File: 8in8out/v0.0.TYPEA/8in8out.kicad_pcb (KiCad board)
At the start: 2 copper layers, 100.1 x 86.4 mm, 63 parts, among them IC1 ATTINY48-A, J1 RJ45, J2 RJ45, J3 CONN_6, K110 G5T-1-12VDC, K120 G5T-1-12VDC, K130 G5T-1-12VDC, K140 G5T-1-12VDC, K150 G5T-1-12VDC, K160 G5T-1-12VDC, K170 G5T-1-12VDC, K180 G5T-1-12VDC, P1 CONN_5, P100 CONN_2, P101 CONN_2, P102 CONN_2, P103 CONN_2, P105 CONN_2, P106 CONN_2, P110 CONN_2, P120 CONN_2, P130 CONN_2, P140 CONN_2, P150 CONN_2, P160 CONN_2, P170 CONN_2, P180 CONN_2, P2 CONN_5, P3 CONN_10X2, P4 CONN_2, U1 7805, U10 OPTO-TRANSISTOR, U2 ULN2803, U20 OPTO-TRANSISTOR, U30 OPTO-TRANSISTOR, U40 OPTO-TRANSISTOR, U50 OPTO-TRANSISTOR, U60 OPTO-TRANSISTOR, U70 OPTO-TRANSISTOR, U80 OPTO-TRANSISTOR

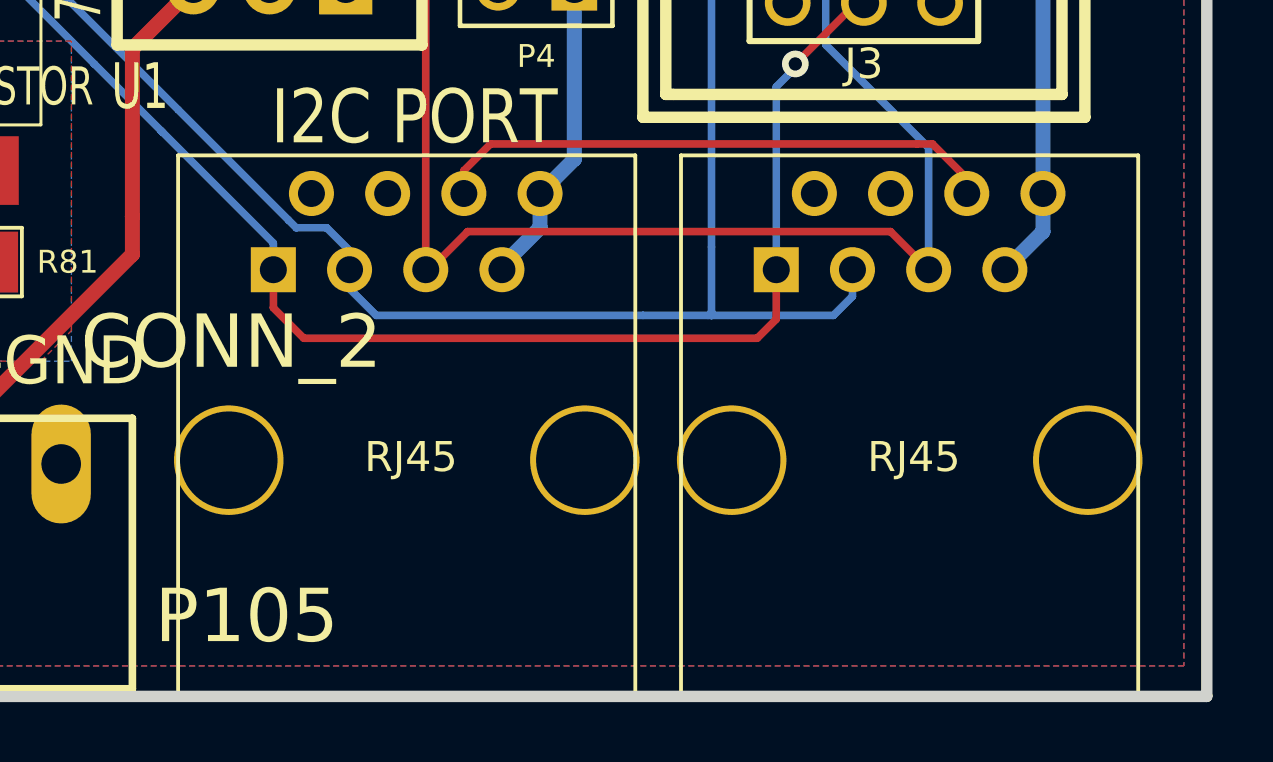
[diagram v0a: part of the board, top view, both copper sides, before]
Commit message: correction empreinte relais (inversion broches du contact) correction empreinte RJ45 (ajout percage shield)
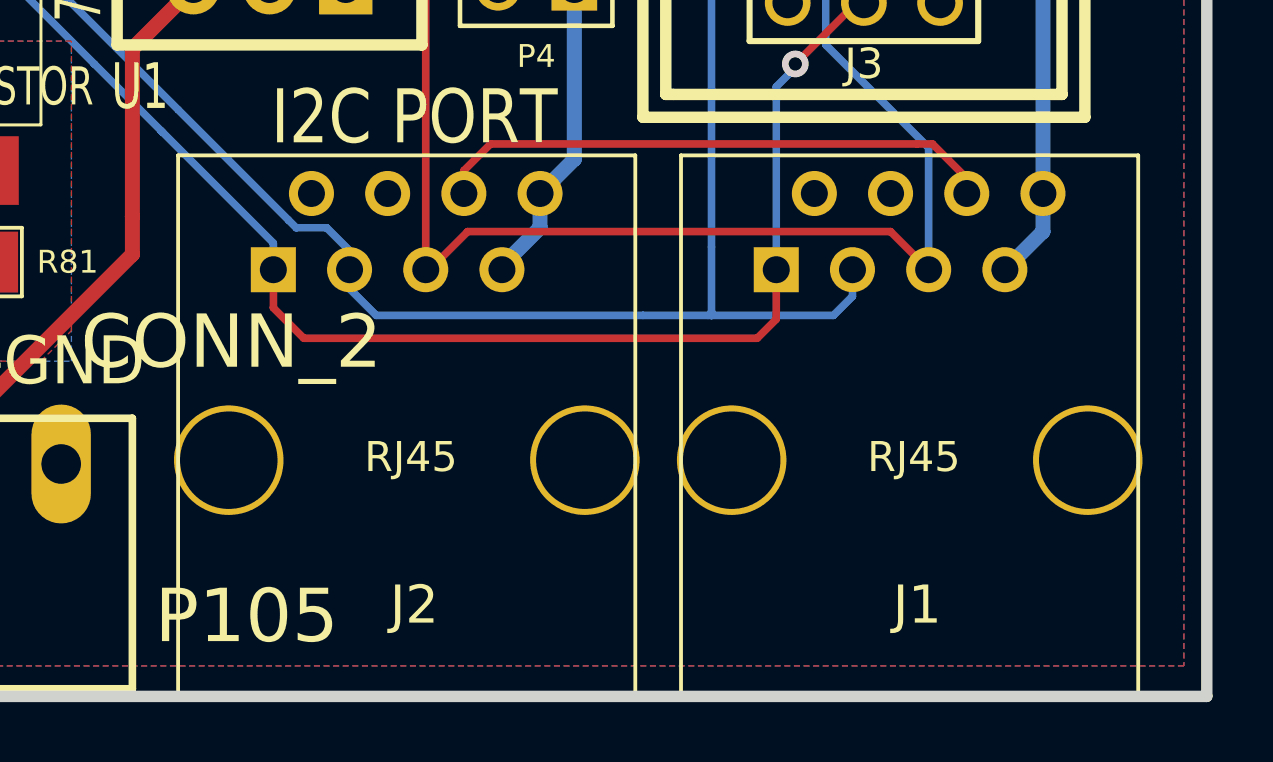
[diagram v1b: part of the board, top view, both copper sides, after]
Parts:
- J1, J2: footprint RJ45_8 -> RJ45_BASIC
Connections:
- J3 pad 6: (no net) -> N-0000091
- U10 pad 3: (no net) -> N-0000076
- U10 pad 6: (no net) -> N-0000077
- U20 pad 3: (no net) -> N-0000083
- U20 pad 6: (no net) -> N-0000084
- U30 pad 3: (no net) -> N-0000086
- U30 pad 6: (no net) -> N-0000087
- U40 pad 3: (no net) -> N-0000057
- U40 pad 6: (no net) -> N-0000058
- U50 pad 3: (no net) -> N-0000059
- U50 pad 6: (no net) -> N-0000060
- U60 pad 3: (no net) -> N-0000063
- U60 pad 6: (no net) -> N-0000048
- U70 pad 3: (no net) -> N-0000050
- U70 pad 6: (no net) -> N-0000051
- U80 pad 3: (no net) -> N-0000053
- U80 pad 6: (no net) -> N-0000054

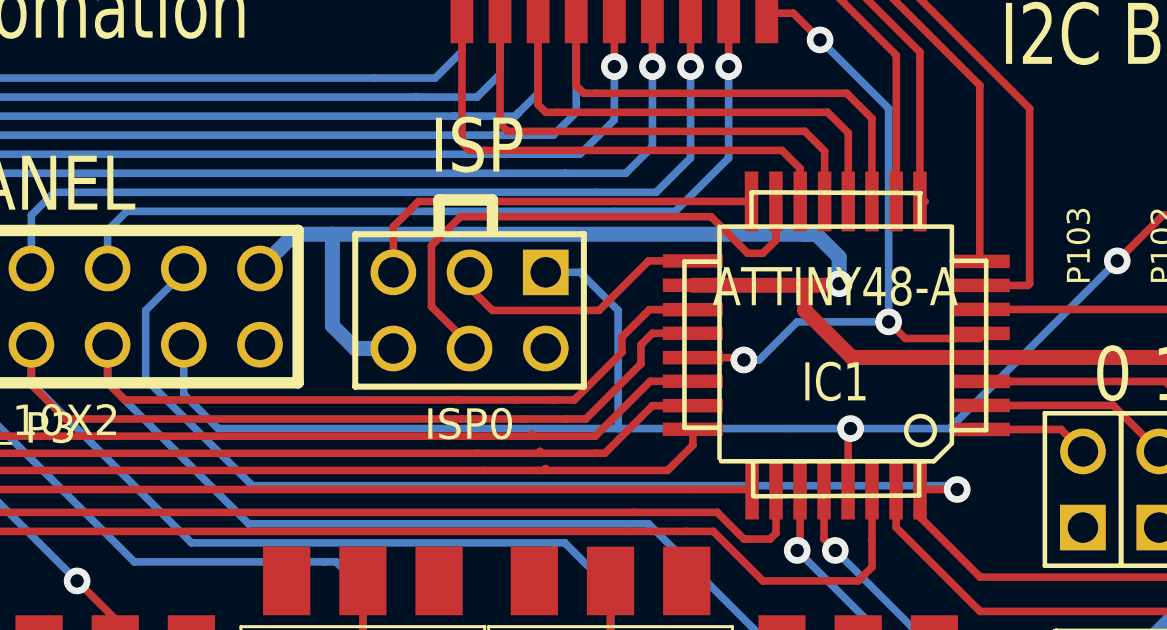
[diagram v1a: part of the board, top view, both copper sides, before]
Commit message: correction connecteur ISP
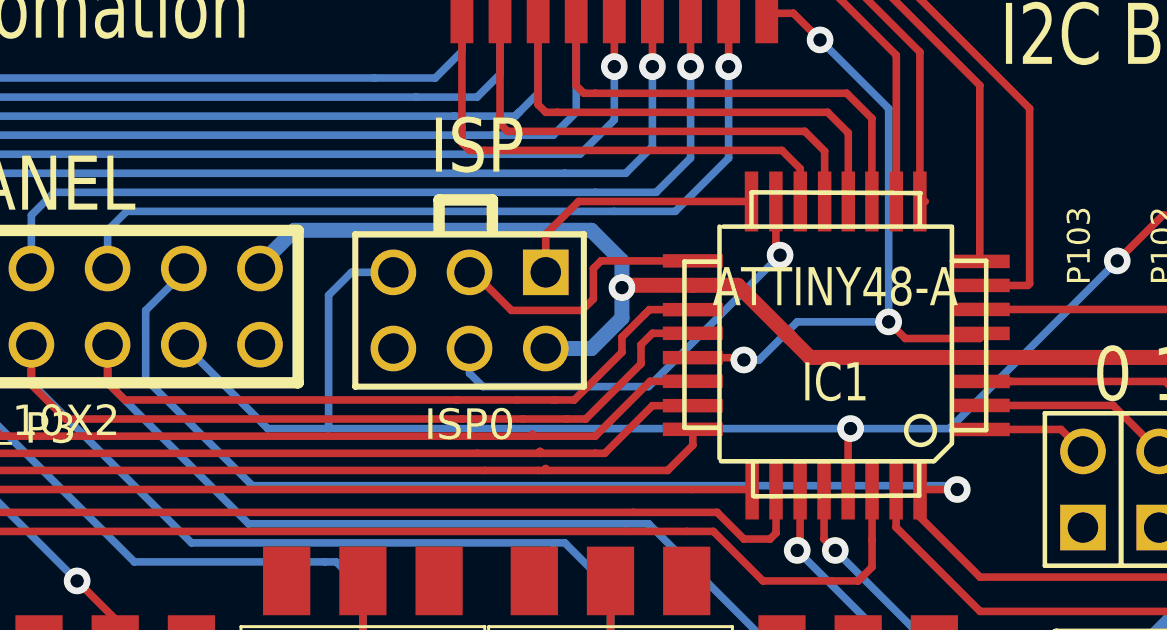
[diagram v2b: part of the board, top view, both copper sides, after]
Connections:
- ISP0 pad 1: RESET -> MISO
- ISP0 pad 2: GND -> +5V
- ISP0 pad 5: MISO -> RESET
- ISP0 pad 6: +5V -> GND
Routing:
- net +5V: track 101.7 -> 93.8 mm
- net MISO: track 13.8 -> 8.58 mm
- net MOSI: track 17.8 -> 15.0 mm, vias 0 -> 1
- net RESET: track 66.0 -> 65.1 mm
